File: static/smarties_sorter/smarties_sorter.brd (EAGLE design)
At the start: 170.2 x 100 mm, 17 parts, among them IC1 MEGA8-P, Q1 16Mhz, Q2 IRLZ44Z

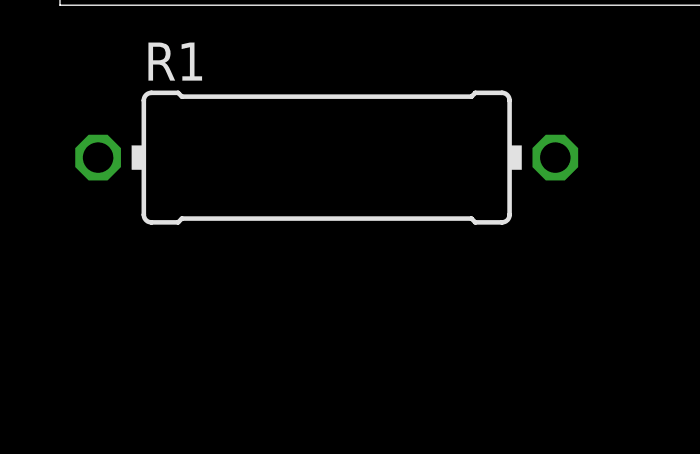
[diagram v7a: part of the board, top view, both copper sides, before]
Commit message: [smarties_sorter] Adds UART plug
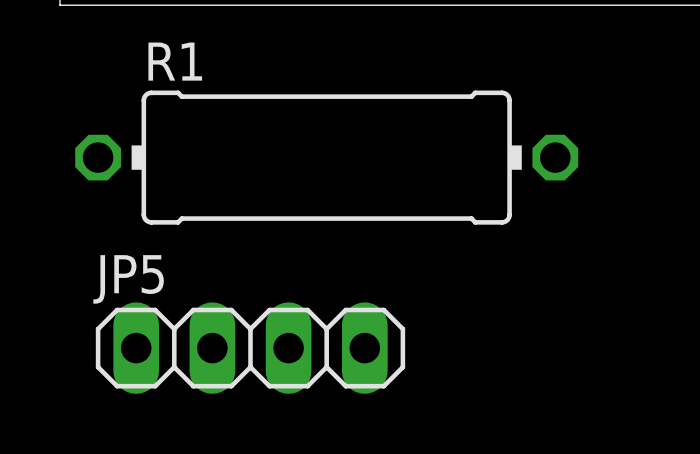
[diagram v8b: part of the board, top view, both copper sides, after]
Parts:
- added JP5: (no value), pinhead:1X04
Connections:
- new net N$13: IC1.2, JP5.4
- new net N$8: IC1.3, JP5.3
- net 5V: now also JP5.1
- net GND: now also JP5.2
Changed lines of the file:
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@@
 <element name="JP4" library="pinhead" package="1X05" value="" x="55.88" y="59.69" rot="R270"/>
 <element name="R1" library="rcl" package="0414/15" value="10Kohms" x="8.89" y="-5.08"/>
+<element name="JP5" library="pinhead" package="1X04" value="" x="6.35" y="-11.43"/>
 </elements>
 <signals>
@@
 <contactref element="JP4" pad="2"/>
 <contactref element="R1" pad="2"/>
+<contactref element="JP5" pad="2"/>
+<wire x1="5.08" y1="-11.43" x2="16.51" y2="-5.08" width="0" layer="19" extent="1-1"/>
 <wire x1="55.88" y1="62.23" x2="16.51" y2="-5.08" width="0" layer="19" extent="1-1"/>
 <wire x1="49.53" y1="67.31" x2="55.88" y2="62.23" width="0" layer="19" extent="16-16"/>
@@
 <wire x1="55.88" y1="66.04" x2="57.15" y2="67.31" width="0.8128" layer="16"/>
 <wire x1="57.15" y1="67.31" x2="60.96" y2="67.31" width="0.8128" layer="16"/>
+<contactref element="JP5" pad="1"/>
 <wire x1="110.49" y1="67.31" x2="102.87" y2="67.31" width="0" layer="19" extent="16-16"/>
+<wire x1="2.54" y1="-11.43" x2="52.07" y2="31.75" width="0" layer="19" extent="16-16"/>
 </signal>
 <signal name="N$6">
@@
 <wire x1="55.88" y1="54.61" x2="96.52" y2="50.8" width="0" layer="19" extent="1-1"/>
 </signal>
+<signal name="N$8">
+<contactref element="IC1" pad="3"/>
+<contactref element="JP5" pad="3"/>
+<wire x1="7.62" y1="-11.43" x2="71.12" y2="50.8" width="0" layer="19" extent="1-1"/>
+</signal>
+<signal name="N$13">
+<contactref element="JP5" pad="4"/>
+<contactref element="IC1" pad="2"/>
+<wire x1="10.16" y1="-11.43" x2="68.58" y2="50.8" width="0" layer="19" extent="1-1"/>
+</signal>
 </signals>
